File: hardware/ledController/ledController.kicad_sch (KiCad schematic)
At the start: 23 parts, among them IC1 PIC16F1769-I_ML, J1 Conn_01x06, J2 Screw_Terminal_01x02, J3 Screw_Terminal_01x02, J4 Conn_01x06, J5 Conn_01x02_Male

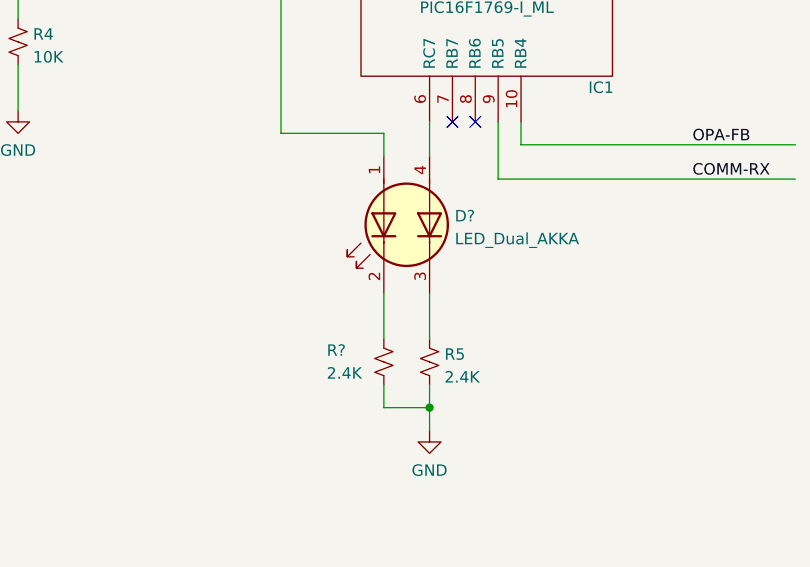
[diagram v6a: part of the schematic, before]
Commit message: modified footprint for D1
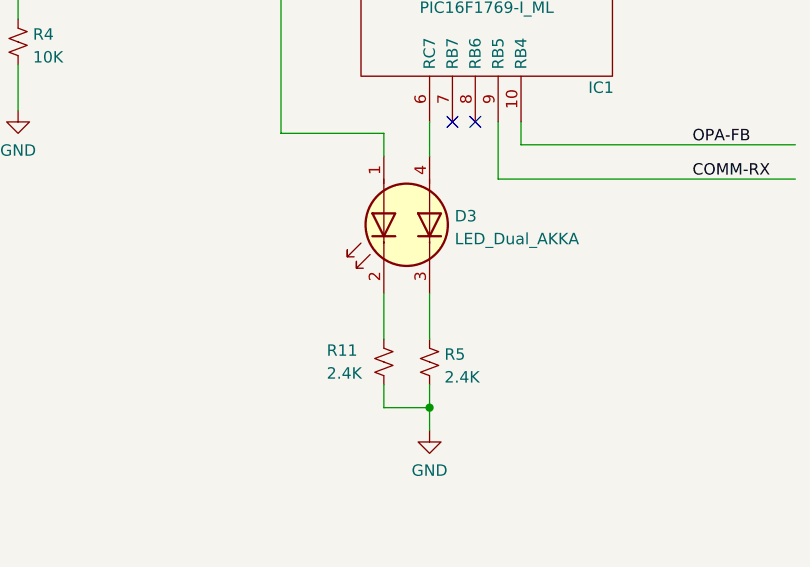
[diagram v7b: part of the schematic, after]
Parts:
- D1: footprint Diode_SMD:D_SMC -> Diode_SMD:D_SMA
- gave numbers to parts that had none: 2
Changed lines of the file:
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@@
   (symbol (lib_id "Device:R_Small_US") (at 187.96 140.97 0) (unit 1)
     (in_bom yes) (on_board yes)
-    (property "Reference" "R?" (id 0) (at 181.61 139.7 0)
+    (property "Reference" "R11" (id 0) (at 181.61 139.7 0)
       (effects (font (size 1.27 1.27)) (justify left))
     )
@@
     (property "Reference" "D1" (id 0) (at 43.4975 82.6602 0))
     (property "Value" "B340" (id 1) (at 43.4975 85.1971 0))
-    (property "Footprint" "Diode_SMD:D_SMC" (id 2) (at 43.18 83.185 0)
+    (property "Footprint" "Diode_SMD:D_SMA" (id 2) (at 43.18 83.185 0)
       (effects (font (size 1.27 1.27)) hide)
     )
@@
   (symbol (lib_id "Device:LED_Dual_AKKA") (at 190.5 125.73 90) (mirror x) (unit 1)
     (in_bom yes) (on_board yes) (fields_autoplaced)
-    (property "Reference" "D?" (id 0) (at 195.834 124.7683 90)
+    (property "Reference" "D3" (id 0) (at 195.834 124.7683 90)
       (effects (font (size 1.27 1.27)) (justify right))
     )
@@
     )
     (path "/550caa41-c6c7-4ca7-ad95-cdf830f669fd"
-      (reference "D1") (unit 1) (value "B340") (footprint "Diode_SMD:D_SMC")
+      (reference "D1") (unit 1) (value "B340") (footprint "Diode_SMD:D_SMA")
     )
     (path "/a7df80c0-2e6d-4c17-9294-da09aa165e49"
@@
     )
     (path "/66c50902-9d0c-447a-90de-d45899b9f06c"
-      (reference "D?") (unit 1) (value "LED_Dual_AKKA") (footprint "LED_SMD:LED_Kingbright_APHBM2012_2x1.25mm")
+      (reference "D3") (unit 1) (value "LED_Dual_AKKA") (footprint "LED_SMD:LED_Kingbright_APHBM2012_2x1.25mm")
     )
     (path "/31243e06-0979-4fae-860f-4cad80206009"
@@
     )
     (path "/3c0907ef-a933-4de9-8705-d6d11137d646"
-      (reference "R?") (unit 1) (value "2.4K") (footprint "Resistor_SMD:R_0603_1608Metric_Pad0.98x0.95mm_HandSolder")
+      (reference "R11") (unit 1) (value "2.4K") (footprint "Resistor_SMD:R_0603_1608Metric_Pad0.98x0.95mm_HandSolder")
     )
     (path "/04b0a461-f9a3-4e36-bb78-ad096b231c16"

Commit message: Replaced footprint of D2
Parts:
- D2: footprint Package_TO_SOT_SMD:SOT-523 -> ym-footprints:SC-75
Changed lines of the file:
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@@
       (effects (font (size 1.27 1.27)) (justify right))
     )
-    (property "Footprint" "Package_TO_SOT_SMD:SOT-523" (id 2) (at 120.65 53.34 0)
+    (property "Footprint" "ym-footprints:SC-75" (id 2) (at 120.65 53.34 0)
       (effects (font (size 1.27 1.27)) hide)
     )
@@
     )
     (path "/a7df80c0-2e6d-4c17-9294-da09aa165e49"
-      (reference "D2") (unit 1) (value "RCLAMP0502BA") (footprint "Package_TO_SOT_SMD:SOT-523")
+      (reference "D2") (unit 1) (value "RCLAMP0502BA") (footprint "ym-footprints:SC-75")
     )
     (path "/66c50902-9d0c-447a-90de-d45899b9f06c"
